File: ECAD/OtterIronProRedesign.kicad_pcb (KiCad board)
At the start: 2 copper layers, 71 parts, among them J1 Conn_01x01, J2 Conn_01x01, J4 Conn_02x03_Odd_Even, J5 Conn_01x14, J6 USB_C_Receptacle_USB2.0, Q1 NPN 1A 40V, Q2 NPN 1A 40V, Q3 PNP 1A 40V, Q4 NMOS 40V 10A, SW1 SW_Push, SW2 SW_Push, U1 STM32F072C8Ux, U2 STM32F071C8Tx, U3 USBLC6-4SC6, U4 STUSB4500QTR, U5 AP2204R-3.3, U6 MCP6L91T-EOT, U7 MCP9700AT-ETT, U8 INA194

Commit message: routing almost done
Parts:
- removed the C5 at (148.9, 94.2)
- removed the C6 at (152.3, 91.2)
- removed J5: Conn_01x14, OtterIronPro_UiBoard:0.69OLED
- removed Jr: Conn_01x06, OtterIronPro_UiBoard:RPC1-12RB-6P(71)
- removed NT10, NT11, NT12, NT5, NT6, NT7, NT9: Net-Tie_2, NetTie:NetTie-2_SMD_Pad0.5mm
- removed NT8: Net-Tie_2, NetTie:NetTie-2_SMD_Pad2.0mm
- removed Q3: PNP 1A 40V, Package_TO_SOT_SMD:SOT-23
- removed Q4: NMOS 40V 10A, Package_TO_SOT_SMD:TO-252-2
- removed R15: 0, Resistor_SMD:R_0402_1005Metric
- removed R16: 10k, Resistor_SMD:R_0402_1005Metric
- removed R17: 33, Resistor_SMD:R_0402_1005Metric
- removed R18: 20m 0.5W, Resistor_SMD:R_1206_3216Metric
- removed R3: 560k, Resistor_SMD:R_0402_1005Metric
- removed the R7 at (143.1, 94.2)
- removed U7: MCP9700AT-ETT, Package_TO_SOT_SMD:SOT-23
- removed U8: INA194, Package_TO_SOT_SMD:SOT-23-5
- added C19: 1µF 35V, Capacitor_SMD:C_0402_1005Metric, B.Cu at (120.5, 95.0)
- added C20: 1µF 35V, Capacitor_SMD:C_0402_1005Metric, B.Cu at (151.5, 101.5)
- added C22: 1µF 35V, Capacitor_SMD:C_0402_1005Metric, B.Cu at (149.5, 101.5)
- added C23: 100nF, Capacitor_SMD:C_0402_1005Metric, B.Cu at (112.5, 97.0)
- added C24: 1µF 35V, Capacitor_SMD:C_0402_1005Metric, B.Cu at (117.0, 89.0)
- added C3: 100nF, Capacitor_SMD:C_0402_1005Metric, B.Cu at (139.8, 103.3)
- added C32: 100nF, Capacitor_SMD:C_0402_1005Metric, B.Cu at (145.0, 89.5)
- added C33: 100nF, Capacitor_SMD:C_0402_1005Metric, B.Cu at (145.0, 98.0)
- added C34: 1µF 35V, Capacitor_SMD:C_0402_1005Metric, B.Cu at (118.5, 105.0)
- added C35: 1µF 35V, Capacitor_SMD:C_0402_1005Metric, B.Cu at (120.5, 105.0)
- added C36: 100µF 35V, Capacitor_SMD:CP_Elec_10x10.5, B.Cu at (129.0, 107.0)
- added C4: 100nF, Capacitor_SMD:C_0402_1005Metric, B.Cu at (149.2, 108.9)
- added H1: MountingHole, MountingHole:MountingHole_3.2mm_M3, F.Cu at (175.0, 90.0)
- added H4: MountingHole, MountingHole:MountingHole_3.2mm_M3, F.Cu at (175.0, 110.0)
- added J11: Conn_01x01, TestPoint:TestPoint_Pad_3.0x3.0mm, F.Cu at (107.7, 94.0)
- added J12: Conn_01x01, TestPoint:TestPoint_Pad_3.0x3.0mm, B.Cu at (107.7, 94.0)
- added J14: Conn_01x01, TestPoint:TestPoint_Pad_3.0x3.0mm, F.Cu at (107.7, 90.0)
- added J16: Conn_01x01, TestPoint:TestPoint_Pad_3.0x3.0mm, B.Cu at (107.7, 90.0)
- added J17: Conn_01x01, TestPoint:TestPoint_Pad_3.0x3.0mm, F.Cu at (107.7, 98.0)
- added J19: Conn_01x01, TestPoint:TestPoint_Pad_3.0x3.0mm, B.Cu at (107.7, 98.0)
- added J20: Conn_01x01, TestPoint:TestPoint_Keystone_5019_Minature, B.Cu at (170.5, 90.0)
- added J21: Conn_01x01, TestPoint:TestPoint_Keystone_5019_Minature, B.Cu at (157.0, 106.5)
- added J22: Conn_01x01, TestPoint:TestPoint_Keystone_5019_Minature, B.Cu at (170.5, 110.0)
- added J23: Conn_02x03_Odd_Even, Connector:Tag-Connect_TC2030-IDC-NL_2x03_P1.27mm_Vertical, B.Cu at (138.0, 109.0)
- added J24: Conn_01x14, OtterIronPro_UiBoard:0.69OLED, B.Cu at (158.5, 100.0)
- added J25: USB_C_Receptacle_USB2.0, Connector_USB:USB_C_Receptacle_XKB_U262-16XN-4BVC11, B.Cu at (177.5, 100.0)
- added J8: Conn_01x01, TestPoint:TestPoint_Pad_3.0x3.0mm, F.Cu at (107.7, 102.0)
- added J9: Conn_01x01, TestPoint:TestPoint_Pad_3.0x3.0mm, B.Cu at (107.7, 102.0)
- added L1: 1µH 15A, Inductor_SMD:L_12x12mm_H8mm, B.Cu at (136.5, 94.5)
- added R21: 1k, Resistor_SMD:R_0402_1005Metric, B.Cu at (145.5, 96.5)
- added R22: 8m ±1% 2W ±100ppm/°C, Resistor_SMD:R_2512_6332Metric, B.Cu at (147.5, 93.5)
- added R5: 10k, Resistor_SMD:R_0402_1005Metric, B.Cu at (139.0, 101.0)
- added R6: 1M, Diode_SMD:D_0402_1005Metric, B.Cu at (160.0, 106.5)
- added U9: INA194, Package_TO_SOT_SMD:SOT-23-5, B.Cu at (147.5, 89.7)
- C1, C10, C11, C12, C13, C14, C16, C17, C7, C8, NT2, NT3, NT4, R1, R10, R11, R2, R8, SW1, SW2, U1, U3, U5: moved to B.Cu
- C15: value 1µF 35V -> 100nF; moved to B.Cu
- C18: value 470µF 35V -> 1µF 35V; footprint Capacitor_SMD:CP_Elec_10x10.5 -> Capacitor_SMD:C_0402_1005Metric; moved to B.Cu
- C2: value 470µF 35V -> 100nF; footprint Capacitor_SMD:CP_Elec_10x10.5 -> Capacitor_SMD:C_0402_1005Metric; moved to B.Cu
- C21, C9: value 100nF -> 1µF 35V; moved to B.Cu
- C5: renamed from C3; moved to B.Cu
- C6: renamed from C4; moved to B.Cu
- D1: value 30V 10A -> 24V 10A; moved to B.Cu
- D2: value 22V 10A -> D; footprint Diode_SMD:D_SMB -> Diode_SMD:D_SMA; moved to B.Cu
- F1: value 4A fast blowing -> 10A fast blowing; moved to B.Cu
- J1: footprint Connector_Wire:SolderWire-0.5sqmm_1x01_D0.9mm_OD2.3mm -> TestPoint:TestPoint_Pad_3.0x3.0mm
- J2: footprint Connector_Wire:SolderWire-0.5sqmm_1x01_D0.9mm_OD2.3mm -> TestPoint:TestPoint_Pad_3.0x3.0mm; moved to B.Cu
- J4: value Conn_02x03_Odd_Even -> Conn_01x01; footprint Connector:Tag-Connect_TC2030-IDC-NL_2x03_P1.27mm_Vertical -> TestPoint:TestPoint_Pad_3.0x3.0mm
- J6: value USB_C_Receptacle_USB2.0 -> Conn_01x01; footprint Connector_USB:USB_C_Receptacle_XKB_U262-16XN-4BVC11 -> TestPoint:TestPoint_Pad_3.0x3.0mm; moved to B.Cu
- NT1: footprint NetTie:NetTie-2_SMD_Pad2.0mm -> NetTie:NetTie-2_SMD_Pad0.5mm; moved to B.Cu
- Q1, Q2: value NPN 1A 40V -> Q_NMOS_GDS; footprint Package_TO_SOT_SMD:SOT-23 -> Package_TO_SOT_SMD:TO-252-2; moved to B.Cu
- R12, R13: value 10k -> 2.2; moved to B.Cu
- R14: value 33 -> 2.2; moved to B.Cu
- R4: value R -> 68k; moved to B.Cu
- R7: renamed from R6; moved to B.Cu
- R9: value 10k -> 560k; moved to B.Cu
- U2: value STM32F071C8Tx -> STUSB4500QTR; footprint Package_QFP:LQFP-48_7x7mm_P0.5mm -> Package_DFN_QFN:QFN-24-1EP_4x4mm_P0.5mm_EP2.7x2.7mm; moved to B.Cu
- U4: value STUSB4500QTR -> L7809; footprint Package_DFN_QFN:QFN-24-1EP_4x4mm_P0.5mm_EP2.7x2.7mm -> Package_TO_SOT_SMD:TO-252-2; moved to B.Cu
- U6: value MCP6L91T-EOT -> LM5109AMA; footprint Package_TO_SOT_SMD:SOT-23-5 -> Package_SO:SOIC-8_3.9x4.9mm_P1.27mm; moved to B.Cu
- moved Q2 120.2 mm to (116.0, 101.0), turned to 180 degrees
- moved Q1 118.9 mm to (116.0, 109.0)
- moved R13 100.7 mm to (116.0, 105.0)
- moved R12 99.2 mm to (115.0, 89.0), turned to 180 degrees
- moved C18 98.3 mm to (121.0, 96.5), turned to 90 degrees
- moved U3 93.7 mm to (170.2, 101.4), turned to 90 degrees
- moved C17 93.4 mm to (129.0, 96.0), turned to 90 degrees
- moved R14 91.4 mm to (119.7, 96.5), turned to 90 degrees
- moved R10 82.9 mm to (169.9, 106.4), turned to 45 degrees
- moved C10 76.3 mm to (155.2, 102.0), turned to 0 degrees
- moved C9 76.0 mm to (155.2, 104.0), turned to 180 degrees
- moved C11 72.0 mm to (155.0, 96.7), turned to 180 degrees
- moved R9 71.8 mm to (153.5, 96.6)
- moved C16 71.6 mm to (161.7, 106.9), turned to 180 degrees
- moved R11 70.6 mm to (161.8, 112.0), turned to 180 degrees
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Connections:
- C10 pad 1: /USB/VBusIn -> Net-(C10-Pad1)
- C10 pad 2: GND -> Net-(C10-Pad2)
- C11 pad 1: GND -> Net-(C11-Pad1)
- C11 pad 2: Net-(C11-Pad2) -> GND
- C12 pad 1: GND -> Net-(C12-Pad1)
- C12 pad 2: Net-(C12-Pad2) -> GND
- C13 pad 1: VBUS -> GND
- C13 pad 2: GND -> Net-(C13-Pad2)
- C14 pad 1: +3V3 -> GND
- C14 pad 2: GND -> Net-(C14-Pad2)
- C15 pad 1: +3V3 -> /USB/VBusIn
- C16 pad 1: /PowerStage/Current+ -> /USB/VBusIn
- C16 pad 2: Net-(C16-Pad2) -> GND
- C17 pad 1: /PowerStage/Current+ -> VBUS
- C17 pad 2: Net-(C16-Pad2) -> GND
- C18 pad 1: /PowerStage/Current+ -> +9V
- C18 pad 2: Net-(C16-Pad2) -> GND
- C2 pad 1: VBUS -> +3V3
- C21 pad 1: /CurrentSensing/V+ -> +3V3
- C21 pad 2: /CurrentSensing/GND -> GND
- C7 pad 1: Net-(C7-Pad1) -> +3V3
- C7 pad 2: Net-(C7-Pad2) -> GND
- C8 pad 1: Net-(C8-Pad1) -> +3V3
- C9 pad 1: /USB/VBusIn -> Net-(C9-Pad1)
- C9 pad 2: GND -> Net-(C9-Pad2)
- D1 pad 1: VBUS -> /CurrentSensing/CurrentIn
- D2 pad 1: /USB/VBusIn -> Net-(C23-Pad1)
- D2 pad 2: GND -> Net-(D2-Pad2)
- F1 pad 1: VBUS -> /CurrentSensing/CurrentIn
- F1 pad 2: Net-(F1-Pad2) -> /USB/VBusIn
- J1 pad 1: /USB/VBusIn -> /PowerStage/Out
- J2 pad 1: GNDA -> /PowerStage/Out
- J4 pad 1: +3V3 -> GND
- NT1 pad 1: VBUS -> +3V3
- NT1 pad 2: /CurrentSensing/Current+ -> +3.3VA
- NT2 pad 1: /STM32/CurrentMeasurement -> GND
- NT2 pad 2: /CurrentSensing/CurrentMeasurement -> GNDA
- NT3 pad 1: /STM32/IronPwm -> Net-(NT3-Pad1)
- NT3 pad 2: /PowerStage/PwmIn -> /CurrentSensing/CurrentIn
- NT4 pad 1: +3.3VA -> Net-(NT4-Pad1)
- NT4 pad 2: /CurrentSensing/V+ -> /InputFilter/BusVoltageUnfiltered
- Q1 pad 2: /PowerStage/Current- -> VBUS
- Q1 pad 3: Net-(Q1-Pad3) -> /PowerStage/Out
- Q2 pad 2: Net-(Q2-Pad2) -> /PowerStage/Out
- Q2 pad 3: /PowerStage/Current+ -> GND
- R10 pad 2: /USB/VBusIn -> GND
- R11 pad 1: Net-(Q1-Pad1) -> Net-(R11-Pad1)
- R11 pad 2: /PowerStage/PwmIn -> /USB/VBusIn
- R12 pad 1: /PowerStage/Current+ -> +9V
- R12 pad 2: Net-(Q1-Pad3) -> Net-(D2-Pad2)
- R13 pad 1: Net-(Q2-Pad1) -> Net-(Q1-Pad1)
- R13 pad 2: Net-(Q1-Pad3) -> Net-(R13-Pad2)
- R14 pad 1: Net-(Q4-Pad1) -> Net-(Q2-Pad1)
- R14 pad 2: Net-(Q2-Pad2) -> Net-(R14-Pad2)
- R4 pad 1: /STM32/VBusMeasurement -> VBUS
- R4 pad 2: GNDA -> /STM32/VBusMeasurement
- R9 pad 1: Net-(R9-Pad1) -> GND
- R9 pad 2: GND -> Net-(J24-Pad12)
- U1 pad 10: /STM32/CurrentMeasurement -> /STM32/VBusMeasurement
- U1 pad 11: /STM32/IronTemperature -> /CurrentSensing/CurrentMeasurement
- U1 pad 12: /STM32/VBusMeasurement -> /STM32/IronTemperature
- U1 pad 13: /STM32/Switch1 -> /STM32/PcbTemperature
- U1 pad 15: /STM32/PcbTemperature -> Net-(U1-Pad15)
- U1 pad 2: /STM32/Switch2 -> Net-(U1-Pad2)
- U1 pad 21: Net-(U1-Pad21) -> /STM32/I2C_SCL
- U1 pad 22: Net-(U1-Pad22) -> /STM32/I2C_SDA
- U1 pad 25: /USB/Alert -> /STM32/~VBusAvailable
- U1 pad 26: Net-(U1-Pad26) -> /STM32/Switch1
- U1 pad 27: Net-(U1-Pad27) -> /USB/Alert
- U1 pad 29: /STM32/IronPwm -> Net-(U1-Pad29)
- U1 pad 3: Net-(U1-Pad3) -> /STM32/Switch2
- U1 pad 42: /STM32/I2C_SCL -> /STM32/IronPwmL
- U1 pad 43: /STM32/I2C_SDA -> Net-(U1-Pad43)
- U1 pad 45: Net-(U1-Pad45) -> /STM32/IronPwmH
- U2 pad 1: +3V3 -> /USB/CC1
- U2 pad 10: /STM32/CurrentMeasurement -> GND
- U2 pad 11: /STM32/IronTemperature -> Net-(U2-Pad11)
- U2 pad 12: /STM32/VBusMeasurement -> GND
- U2 pad 13: /STM32/Switch1 -> GND
- U2 pad 15: /STM32/PcbTemperature -> Net-(U2-Pad15)
- U2 pad 18: Net-(U2-Pad18) -> Net-(R11-Pad1)
- U2 pad 19: Net-(U2-Pad19) -> /USB/Alert
- U2 pad 2: /STM32/Switch2 -> /USB/CC1
- U2 pad 20: Net-(U2-Pad20) -> /STM32/~VBusAvailable
- U2 pad 21: Net-(U2-Pad21) -> Net-(C13-Pad2)
- U2 pad 22: Net-(U2-Pad22) -> +3V3
- U2 pad 23: GND -> Net-(C14-Pad2)
- U2 pad 24: +3V3 -> /USB/VBusIn
- U2 pad 25: /USB/Alert -> GND
- U2 pad 4: Net-(U2-Pad4) -> /USB/CC2
- U2 pad 5: Net-(U2-Pad5) -> /USB/CC2
- U2 pad 6: Net-(U2-Pad6) -> Net-(R10-Pad1)
- U2 pad 7: Net-(U2-Pad7) -> /STM32/I2C_SCL
- U2 pad 8: GNDA -> /STM32/I2C_SDA
- U2 pad 9: +3.3VA -> Net-(U2-Pad9)
- U3 pad 1: /USB/CC1 -> /USB/CC2
- U3 pad 3: /USB/CC2 -> /USB/CC1
- U4 pad 1: /USB/CC1 -> VBUS
- U4 pad 2: /USB/CC1 -> GND
- U4 pad 3: Net-(U4-Pad3) -> +9V
- U5 pad 1: VBUS -> +9V
- U6 pad 1: /TemperatureSensing/IronTemperature -> +9V
- U6 pad 2: /CurrentSensing/GND -> /STM32/IronPwmH
- U6 pad 3: Net-(C20-Pad1) -> /STM32/IronPwmL
- U6 pad 4: Net-(U6-Pad4) -> GND
- U6 pad 5: /CurrentSensing/V+ -> Net-(R14-Pad2)
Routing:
- net /STM32/PcbTemperature: track 0.00 -> 52.2 mm, vias 0 -> 10
- net /STM32/IronTemperature: track 0.00 -> 50.7 mm, vias 0 -> 10
- net +3V3: track 0.00 -> 43.2 mm, vias 0 -> 12
- net /STM32/USB_P: track 1.59 -> 44.5 mm, vias 1 -> 2
- net /STM32/USB_N: track 1.59 -> 43.2 mm, vias 1 -> 2
- net /STM32/I2C_SDA: track 0.00 -> 41.1 mm, vias 0 -> 2
- net /STM32/Switch2: track 0.00 -> 39.1 mm, vias 0 -> 3
- net /STM32/I2C_SCL: track 0.00 -> 37.7 mm, vias 0 -> 3
- net /STM32/IronPwmL: track 0.00 -> 34.6 mm, vias 0 -> 2
- net /STM32/IronPwmH: track 0.00 -> 33.4 mm, vias 0 -> 2
- net /USB/VBusIn: track 0.00 -> 26.0 mm, vias 0 -> 25
- net /USB/Alert: track 0.00 -> 18.5 mm
- net /STM32/~VBusAvailable: track 0.00 -> 18.4 mm
- net +9V: track 0.00 -> 17.6 mm, vias 0 -> 4
- net /STM32/Switch1: track 0.00 -> 13.0 mm
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- added copper zone on In1.Cu, net +3.3VA
- added copper zone on In2.Cu, net +3.3VA
- added copper zone on F.Cu, net +3V3
- added copper zone on B.Cu, net +9V
- added copper zone on B.Cu, net /CurrentSensing/CurrentIn
- added copper zone on B.Cu, net /InputFilter/BusVoltageUnfiltered
- added copper zone on B.Cu, net /PowerStage/Out
- added copper zone on In1.Cu, net /STM32/IronTemperature
- added copper zone on In1.Cu, net /STM32/PcbTemperature
- added copper zone on B.Cu, net /USB/VBusIn
- added copper zone on F.Cu, net /USB/VBusIn
- added copper zone on B.Cu, net GND
- added copper zone on F.Cu, net GND
- added copper zone on In1.Cu, net GND
- added copper zone on In2.Cu, net GND
- added copper zone on B.Cu, net GNDA
- added copper zone on F.Cu, net GNDA
- added copper zone on B.Cu, net VBUS
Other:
- board outline added: 74 x 26 mm
- copper layers 2 -> 4
- rule via_min_drill: 0.3 -> 0.2
- rule via_min_size: 0.4 -> 0.45

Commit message: some rearrangements started
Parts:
- moved NT2 18.9 mm to (147.0, 118.5)
- moved C1 16.5 mm to (138.0, 117.5)
- moved R4 16.5 mm to (137.0, 117.5)
- moved R5 16.5 mm to (139.0, 117.5)
- moved U5 16.3 mm to (138.5, 109.5), turned to 180 degrees
- moved NT1 15.5 mm to (149.5, 119.0)
- moved C20 12.2 mm to (141.5, 108.5), turned to 270 degrees
- moved C22 12.0 mm to (141.5, 110.5), turned to 90 degrees
- moved C21 10.6 mm to (142.5, 110.5), turned to 90 degrees
- moved C33 7.02 mm to (152.0, 98.5), turned to 0 degrees
- moved R2 6.96 mm to (155.2, 101.0), turned to 180 degrees
- moved R21 6.02 mm to (151.5, 97.0)
- moved C2 4.30 mm to (145.1, 108.1)
- moved C3 4.30 mm to (143.3, 100.8)
- moved C4 4.30 mm to (152.7, 106.4)
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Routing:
- net /STM32/USB_N: track 43.2 -> 19.7 mm
- net /STM32/USB_P: track 44.5 -> 21.5 mm
- net /STM32/I2C_SDA: track 41.1 -> 26.7 mm
- net /USB/Alert: track 18.5 -> 5.59 mm
- net /STM32/VBusMeasurement: track 13.0 -> 1.98 mm
- net /STM32/IronPwmL: track 34.6 -> 24.5 mm
- net /STM32/IronPwmH: track 33.4 -> 23.9 mm
- net /STM32/Switch2: track 39.1 -> 31.0 mm
- net +3V3: track 43.2 -> 35.6 mm, vias 12 -> 9
- net /STM32/I2C_SCL: track 37.7 -> 30.2 mm, vias 3 -> 1
- net /STM32/SWDIO: track 7.18 -> 0.00 mm, vias 2 -> 0
- net /STM32/PcbTemperature: track 52.2 -> 45.7 mm
- net /CurrentSensing/CurrentMeasurement: track 6.09 -> 0.00 mm
- net /STM32/IronTemperature: track 50.7 -> 45.1 mm
- net /STM32/Switch1: track 13.0 -> 8.43 mm
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
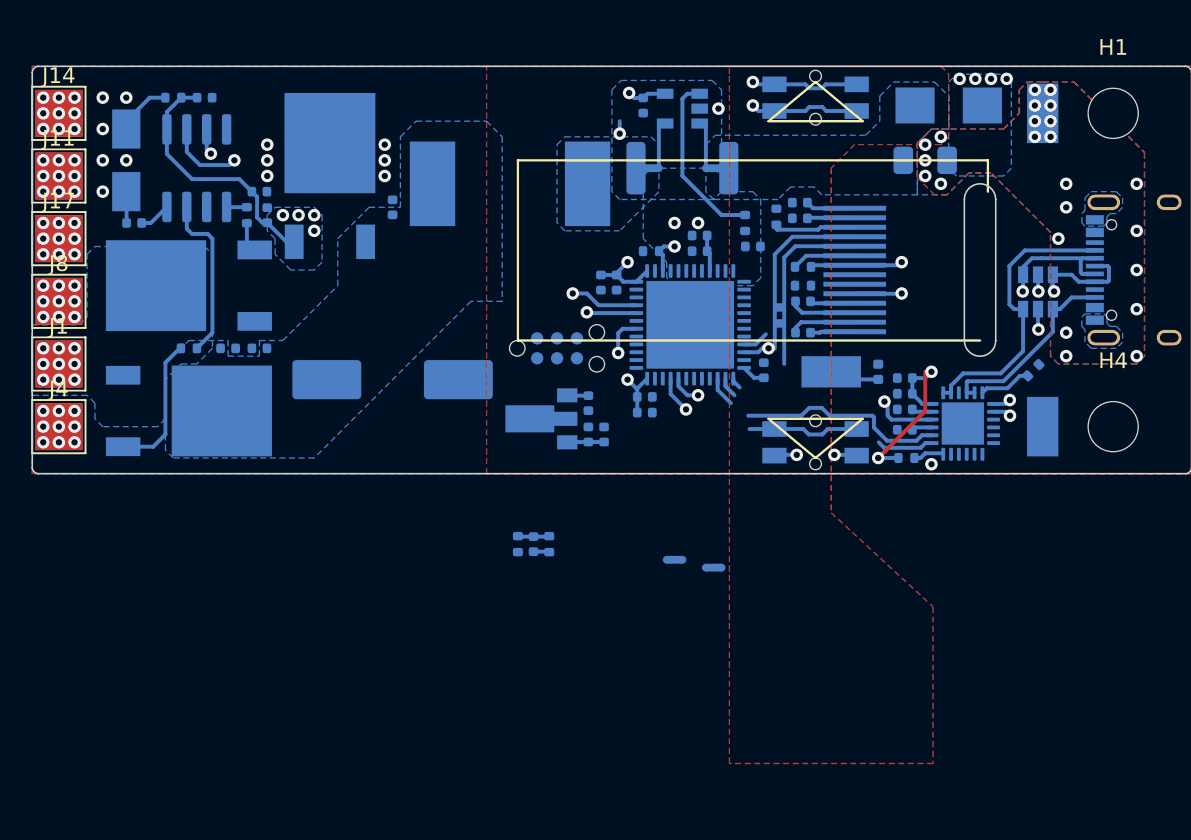
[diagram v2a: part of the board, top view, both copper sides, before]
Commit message: swapped microcontroller
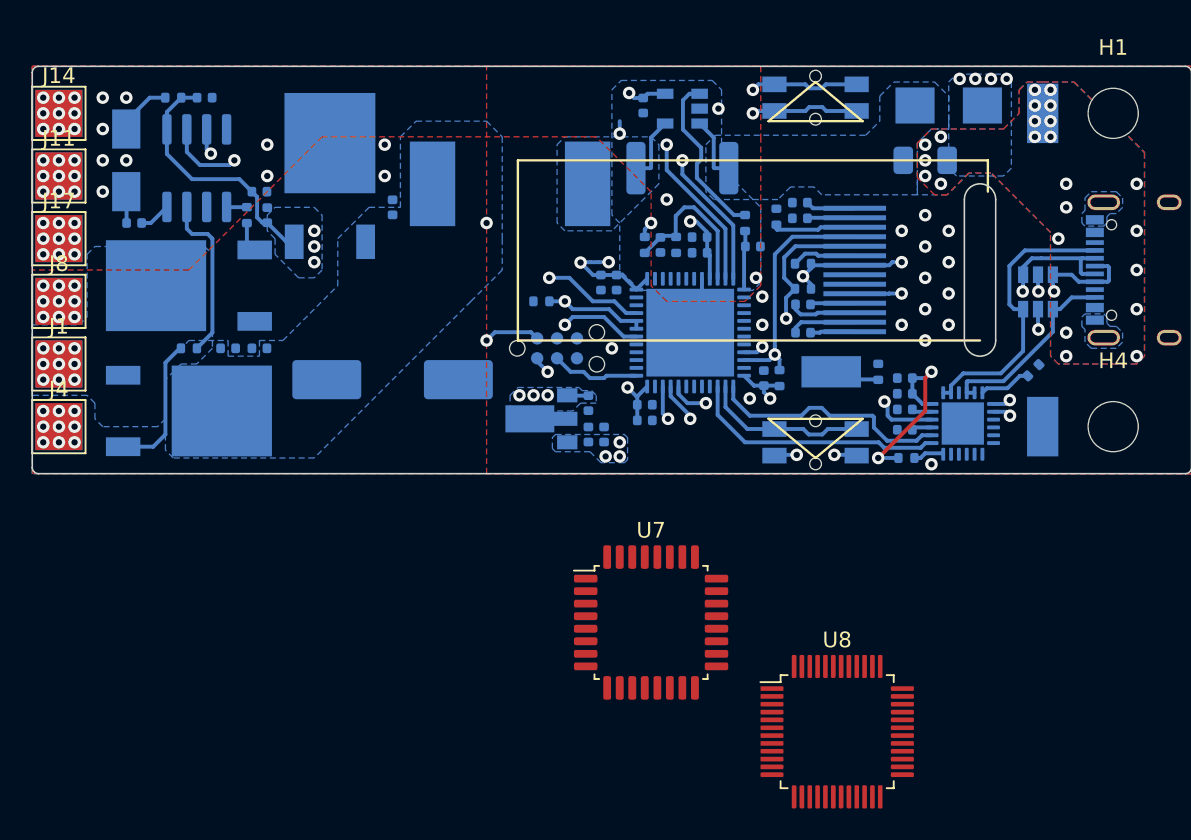
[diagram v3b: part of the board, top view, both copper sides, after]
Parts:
- added U7: STM32F042K6Tx, Package_QFP:LQFP-32_7x7mm_P0.8mm, F.Cu at (145.5, 122.5)
- added U8: STM32F042C6Tx, Package_QFP:LQFP-48_7x7mm_P0.5mm, F.Cu at (157.4, 129.5)
- D1: value 24V 10A -> 20V 10A
- NT1, NT2, NT3, NT4: footprint NetTie:NetTie-2_SMD_Pad0.5mm -> ECAD:NetTie-2_SMD_Pad0.25mm
- R6: footprint Diode_SMD:D_0402_1005Metric -> Resistor_SMD:R_0402_1005Metric
- moved NT1 20.9 mm to (141.9, 99.5)
- moved C1 20.7 mm to (146.1, 98.4)
- moved R4 20.7 mm to (145.1, 98.4), turned to 270 degrees
- moved R5 20.7 mm to (147.1, 98.4)
- moved NT2 17.5 mm to (148.8, 101.1), turned to 90 degrees
- moved R7 7.70 mm to (138.5, 102.0)
- moved R1 4.00 mm to (153.7, 106.9), turned to 90 degrees
- moved C2 0.50 mm to (145.1, 108.6)
- moved C4 0.50 mm to (152.7, 106.9)
- moved C7 0.50 mm to (145.1, 109.6)
- moved U1 0.50 mm to (148.0, 104.0)
- moved NT3 0.30 mm to (149.8, 93.5)
- moved NT4 0.30 mm to (145.2, 93.5)
- moved C10 0.20 mm to (155.2, 102.2)
- moved R2 0.20 mm to (155.2, 101.2)
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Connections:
- U1 pad 11: /CurrentSensing/CurrentMeasurement -> /STM32/IronTemperature
- U1 pad 12: /STM32/IronTemperature -> /STM32/PcbTemperature
- U1 pad 13: /STM32/PcbTemperature -> /CurrentSensing/CurrentMeasurement
- U1 pad 3: /STM32/Switch2 -> Net-(U1-Pad3)
- U1 pad 43: Net-(U1-Pad43) -> /STM32/Switch2
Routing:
- net /STM32/USB_N: track 19.7 -> 41.1 mm
- net /STM32/USB_P: track 21.5 -> 41.4 mm
- net /STM32/SWDIO: track 0.00 -> 12.3 mm, vias 0 -> 2
- net VBUS: track 0.00 -> 11.6 mm, vias 0 -> 2
- net /STM32/IronPwmH: track 23.9 -> 35.4 mm
- net /USB/Alert: track 5.59 -> 16.5 mm
- net /STM32/IronPwmL: track 24.5 -> 35.1 mm
- net /STM32/Switch2: track 31.0 -> 41.1 mm, vias 3 -> 2
- net /STM32/VBusMeasurement: track 1.98 -> 10.2 mm
- net /STM32/I2C_SDA: track 26.7 -> 33.5 mm
- net +3V3: track 35.6 -> 42.2 mm, vias 9 -> 15
- net /STM32/SWCLK: track 0.00 -> 5.65 mm
- net +3.3VA: track 4.88 -> 10.5 mm, vias 14 -> 16
- net /STM32/PcbTemperature: track 45.7 -> 50.7 mm
- net /STM32/IronTemperature: track 45.1 -> 49.7 mm
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- added copper zone on B.Cu, net +3V3
- added copper zone on In1.Cu, net +3V3
- added copper zone on In1.Cu, net +9V
- removed copper zone on F.Cu, net +3V3
- removed copper zone on In1.Cu, net GND

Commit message: forgot to save
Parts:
- removed C4: 100nF, Capacitor_SMD:C_0402_1005Metric
- removed U1: STM32F072C8Ux, Package_DFN_QFN:QFN-48-1EP_7x7mm_P0.5mm_EP5.6x5.6mm
- removed U8: STM32F042C6Tx, Package_QFP:LQFP-48_7x7mm_P0.5mm
- U7: moved to B.Cu
- moved U7 17.7 mm to (148.0, 105.0), turned to 270 degrees
- moved R2 11.5 mm to (149.6, 111.2), turned to 90 degrees
- moved R1 6.67 mm to (148.6, 111.2)
- moved C2 6.36 mm to (151.1, 110.7)
- moved C7 6.36 mm to (151.1, 111.7)
- moved R7 4.03 mm to (142.2, 103.6), turned to 270 degrees
- moved J23 2.06 mm to (138.2, 103.4)
- moved NT2 1.42 mm to (149.0, 102.5)
- moved C1 0.61 mm to (145.5, 98.5)
- moved C5 0.61 mm to (148.0, 99.0)
- moved C6 0.61 mm to (148.0, 98.0)
- moved R4 0.61 mm to (144.5, 98.5)
- moved R5 0.61 mm to (146.5, 98.5)
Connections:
- U7 pad 1: Net-(U7-Pad1) -> +3V3
- U7 pad 12: Net-(U7-Pad12) -> /STM32/~VBusAvailable
- U7 pad 13: Net-(U7-Pad13) -> /STM32/IronPwmL
- U7 pad 14: Net-(U7-Pad14) -> /USB/Alert
- U7 pad 15: Net-(U7-Pad15) -> /STM32/Switch1
- U7 pad 16: Net-(U7-Pad16) -> GND
- U7 pad 17: Net-(U7-Pad17) -> +3V3
- U7 pad 18: Net-(U7-Pad18) -> /STM32/IronPwmH
- U7 pad 19: Net-(U7-Pad19) -> /STM32/I2C_SCL
- U7 pad 20: Net-(U7-Pad20) -> /STM32/I2C_SDA
- U7 pad 21: Net-(U7-Pad21) -> /STM32/USB_N
- U7 pad 22: Net-(U7-Pad22) -> /STM32/USB_P
- U7 pad 23: Net-(U7-Pad23) -> /STM32/SWDIO
- U7 pad 24: Net-(U7-Pad24) -> /STM32/SWCLK
- U7 pad 31: Net-(U7-Pad31) -> /STM32/Switch2
- U7 pad 32: Net-(U7-Pad32) -> GNDA
- U7 pad 5: Net-(U7-Pad5) -> +3.3VA
- U7 pad 6: Net-(U7-Pad6) -> /STM32/VBusMeasurement
- U7 pad 7: Net-(U7-Pad7) -> /STM32/IronTemperature
- U7 pad 8: Net-(U7-Pad8) -> /STM32/PcbTemperature
- U7 pad 9: Net-(U7-Pad9) -> /CurrentSensing/CurrentMeasurement
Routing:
- net /USB/Alert: track 16.5 -> 3.67 mm
- net /STM32/Switch2: track 41.1 -> 29.8 mm
- net /STM32/IronPwmL: track 35.1 -> 27.4 mm
- net +3V3: track 42.2 -> 34.9 mm, vias 15 -> 10
- net /STM32/~VBusAvailable: track 15.5 -> 9.95 mm
- net +3.3VA: track 10.5 -> 5.22 mm, vias 16 -> 15
- net /STM32/SWCLK: track 5.65 -> 10.9 mm, vias 0 -> 2
- net /STM32/IronPwmH: track 35.4 -> 30.5 mm
- net /CurrentSensing/CurrentMeasurement: track 3.78 -> 4.97 mm
- net /STM32/SWDIO: track 12.3 -> 13.4 mm
- net /STM32/I2C_SDA: track 33.5 -> 32.4 mm, vias 2 -> 3
- net /STM32/USB_P: track 41.4 -> 42.4 mm
- net /STM32/Switch1: track 10.6 -> 9.63 mm
- net GNDA: track 1.05 -> 0.84 mm, vias 15 -> 14
- net GND: vias 34 -> 30

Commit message: more routing + some component changes
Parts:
- removed the C5 at (148.0, 99.0)
- removed the C6 at (148.0, 98.0)
- added C2: 100nF, Capacitor_SMD:C_0402_1005Metric, B.Cu at (147.9, 99.3)
- added C3: 1µF 35V, Capacitor_SMD:C_0402_1005Metric, B.Cu at (147.9, 98.3)
- added J3: Conn_01x01, TestPoint:TestPoint_Keystone_5019_Minature, B.Cu at (169.0, 96.5)
- added R3: 68k, Resistor_SMD:R_0402_1005Metric, B.Cu at (144.4, 98.2)
- added SW2: SW_Push, Button_Switch_SMD:SW_Push_1P1T_NO_6x6mm_H9.5mm, F.Cu at (131.0, 100.0)
- R16: renamed from R22; value 8m ±1% 2W ±100ppm/°C -> 4m ±1% 2W ±100ppm/°C
- R4: value 68k -> 10k
- R5: value 10k -> 1M
- U7: renamed from U9; value INA194 -> INA195
- moved R5 24.5 mm to (171.0, 97.5), turned to 90 degrees
- moved NT1 6.31 mm to (147.8, 97.2)
- moved R4 1.92 mm to (146.4, 98.8)
- moved C7 1.40 mm to (142.3, 102.2)
- moved C5 0.94 mm to (144.1, 100.3)
- moved C24 0.70 mm to (152.0, 99.2)
- moved R15 0.70 mm to (151.5, 97.7)
- moved NT2 0.61 mm to (149.1, 103.1)
- moved R7 0.51 mm to (142.3, 104.1)
- moved C1 0.32 mm to (145.4, 98.8)
- moved C16 0.10 mm to (129.1, 96.0)
- moved C17 0.10 mm to (141.6, 108.5)
- moved C19 0.10 mm to (142.6, 110.5)
- moved C21 0.10 mm to (141.6, 110.5)
- moved C4 0.10 mm to (151.0, 110.7)
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- renumbered C9 to C10, C12 to C11, C15 to C12, C16 to C13, C13 to C14, C14 to C15, C17 to C16, C20 to C17, C21 to C19, C19 to C20, C22 to C21, C24 to C22, C33 to C24, C32 to C25, C34 to C26, C35 to C27, C36 to C28, C2 to C4, C3 to C5, C7 to C6, C8 to C7, C10 to C8, C11 to C9, H4 to H2, J20 to J1, J16 to J10, J17 to J11, J19 to J12, J1 to J13, J2 to J14, J4 to J15, J6 to J16, J23 to J17, J24 to J18, J25 to J19, J22 to J2, J21 to J4, J8 to J5, J9 to J6, J11 to J7, J12 to J8, J14 to J9, R21 to R15, R9 to R8, R8 to R9, SW2 to SW3, U7 to U1, U3 to U2, U2 to U3
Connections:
- C5 pad 2: GND -> GNDA
- C7 pad 2: GND -> GNDA
- R4 pad 1: VBUS -> /STM32/VBusMeasurement
- R4 pad 2: /STM32/VBusMeasurement -> GNDA
- R5 pad 1: /STM32/VBusMeasurement -> +3V3
- R5 pad 2: GNDA -> Net-(J3-Pad1)
- U1 pad 14: /USB/Alert -> /STM32/Switch1
- U1 pad 15: /STM32/Switch1 -> /USB/Alert
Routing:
- net /STM32/IronPwmL: track 27.4 -> 42.8 mm
- net /STM32/IronPwmH: track 30.5 -> 45.3 mm
- net /USB/Alert: track 3.67 -> 16.9 mm
- net /STM32/I2C_SDA: track 32.4 -> 45.6 mm
- net +3V3: track 34.9 -> 46.0 mm, vias 10 -> 14
- net /STM32/I2C_SCL: track 31.3 -> 42.0 mm
- net /STM32/~VBusAvailable: track 9.95 -> 15.6 mm
- net /USB/VBusIn: track 26.8 -> 30.4 mm
- net Net-(J3-Pad1): track 0.00 -> 2.20 mm
- net +3.3VA: track 5.22 -> 6.56 mm
- net /STM32/Switch1: track 9.63 -> 10.8 mm
- net /CurrentSensing/CurrentMeasurement: track 4.97 -> 4.27 mm
- net /STM32/USB_N: track 41.0 -> 40.4 mm
- net GNDA: vias 14 -> 22
- net GND: vias 30 -> 35
